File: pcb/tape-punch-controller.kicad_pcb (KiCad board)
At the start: 2 copper layers, 70 x 88 mm, 148 parts, among them J1 Conn_01x06, J2 Conn_01x09, J3 USB_B, J4 Conn_01x16, J5 Conn_01x06, J6 Conn_01x02, J7 Conn_02x03_Odd_Even, J8 Conn_01x04, Q1 IRLML0060, Q10 IRLML0060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

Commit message: pcb: change RV1, RV2 and R10 to be 22k instead of 10k
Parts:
- R10, RV1, RV2: value 10k -> 22k
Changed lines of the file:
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@@
       (effects (font (size 1 1) (thickness 0.15)) (justify mirror))
     )
-    (fp_text value 10k (at 0 -1.27 180) (layer B.Fab)
+    (fp_text value 22k (at 0 -1.27 180) (layer B.Fab)
       (effects (font (size 0.75 0.75) (thickness 0.15)) (justify mirror))
     )
@@
       (effects (font (size 1 1) (thickness 0.15)) (justify mirror))
     )
-    (fp_text value 10k (at 0 3.175 180) (layer B.Fab)
+    (fp_text value 22k (at 0 3.175 180) (layer B.Fab)
       (effects (font (size 1 1) (thickness 0.15)) (justify mirror))
     )
@@
       (effects (font (size 1 1) (thickness 0.15)) (justify mirror))
     )
-    (fp_text value 10k (at 0 3.175) (layer B.Fab)
-      (effects (font (size 1 1) (thickness 0.15)) (justify mirror))
-    )
+    (fp_text value 22k (at 0 3.175) (layer B.Fab)
+      (effects (font (size 1 1) (thickness 0.15)) (justify mirror))
+    )

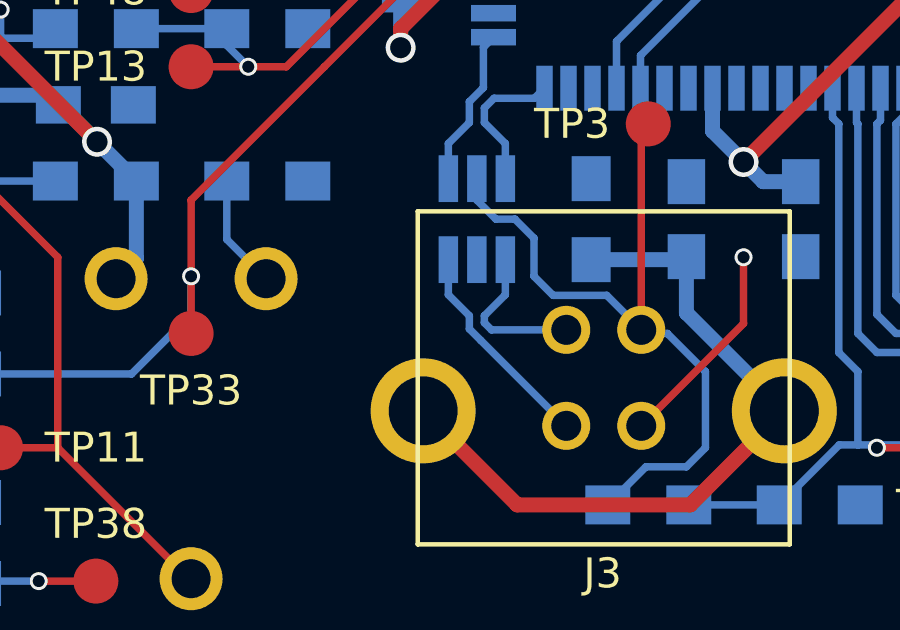
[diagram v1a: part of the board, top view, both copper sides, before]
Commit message: pcb: connect negative side of USB ESD protection IC to USB_SHIELD rather than GND, as per document AVR1017
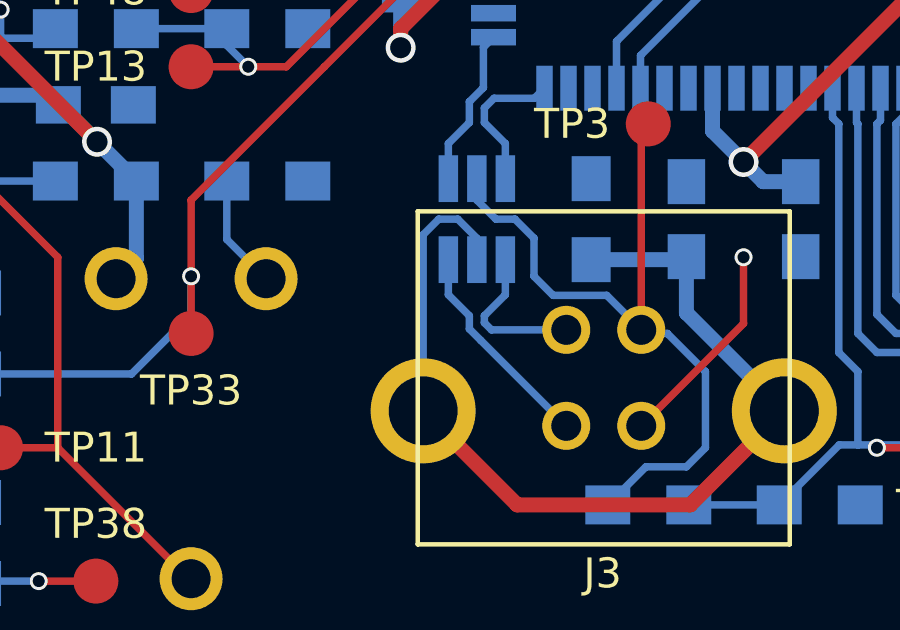
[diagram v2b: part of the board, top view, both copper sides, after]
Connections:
- U3 pad 2: GND -> /Microcontroller/USB_SHIELD
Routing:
- net /Microcontroller/USB_SHIELD: track 24.3 -> 33.2 mm
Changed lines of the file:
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@@
     (thickness 1.6)
     (drawings 78)
-    (tracks 710)
+    (tracks 715)
     (zones 0)
     (modules 148)
@@
       (net 25 /Microcontroller/USB_UNP_D-))
     (pad 2 smd rect (at -1.35 0 90) (size 1.56 0.65) (layers B.Cu B.Paste B.Mask)
-      (net 2 GND))
+      (net 4 /Microcontroller/USB_SHIELD))
     (pad 3 smd rect (at -1.35 -0.95 90) (size 1.56 0.65) (layers B.Cu B.Paste B.Mask)
       (net 24 /Microcontroller/USB_UNP_D+))
@@
   (segment (start 111.205 88.58) (end 114 88.58) (width 0.5) (layer B.Cu) (net 3))
   (segment (start 114 88.58) (end 114.32 88.9) (width 0.5) (layer B.Cu) (net 3))
+  (segment (start 128.27 94.06) (end 128.27 93.345) (width 0.25) (layer B.Cu) (net 4) (status C00000))
+  (segment (start 128.27 93.345) (end 127.635 92.71) (width 0.25) (layer B.Cu) (net 4) (status 400000))
+  (segment (start 127.635 92.71) (end 127 92.71) (width 0.25) (layer B.Cu) (net 4))
+  (segment (start 127 92.71) (end 126.48 93.23) (width 0.25) (layer B.Cu) (net 4))
+  (segment (start 126.48 93.23) (end 126.48 99.1) (width 0.25) (layer B.Cu) (net 4) (status 800000))
   (segment (start 126.48 99.1) (end 129.615 102.235) (width 0.5) (layer F.Cu) (net 4))
   (segment (start 135.385 102.235) (end 138.52 99.1) (width 0.5) (layer F.Cu) (net 4))
